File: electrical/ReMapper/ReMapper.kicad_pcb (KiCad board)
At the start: 4 copper layers, 76.7 x 45.3 mm, 46 parts, among them J2 USB_IN, J5 USB_OUT, U1 ESP32-S3-WROOM-1-N8R8, U2 RP2040, U3 W25Q128JVE, U5 W25Q128JVE, U6 SPX1117M3-L-3-3/TR, Y2 12MHZ

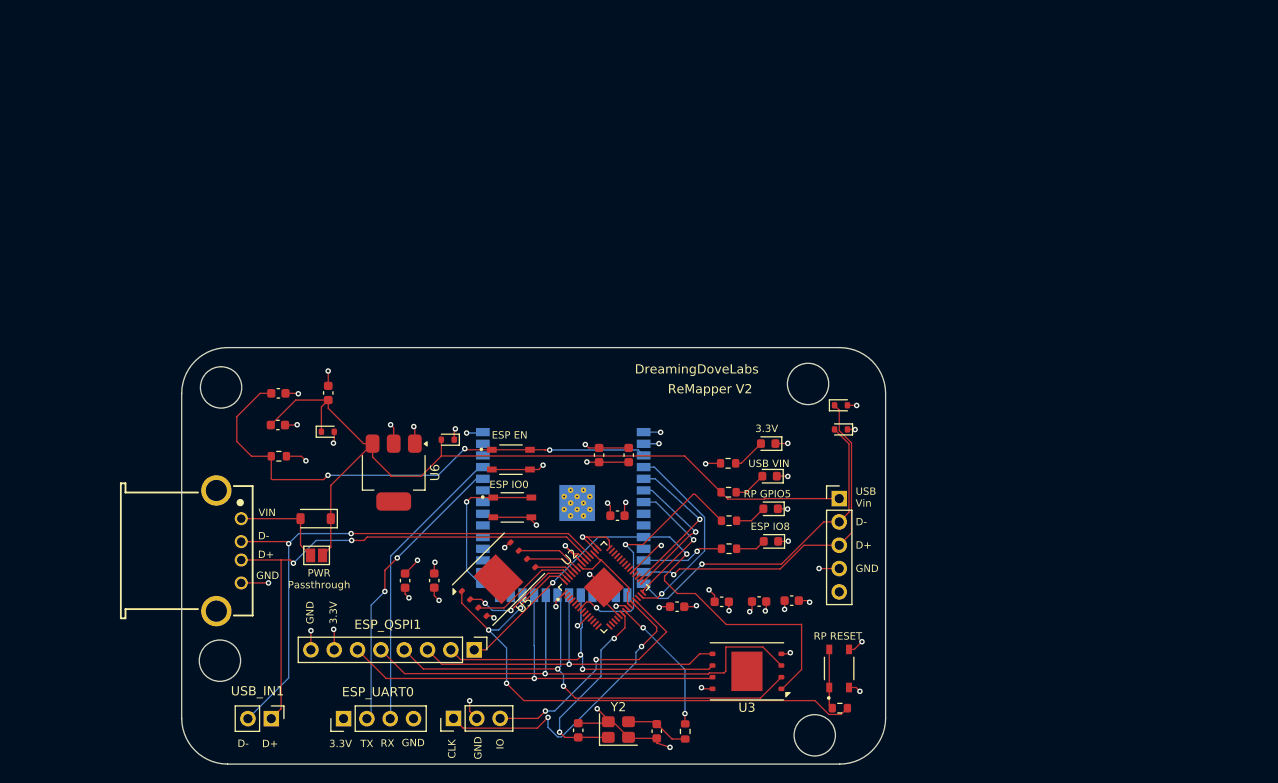
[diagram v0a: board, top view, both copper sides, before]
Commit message: schematic update, pcb design rules and blank slate on pcb editor
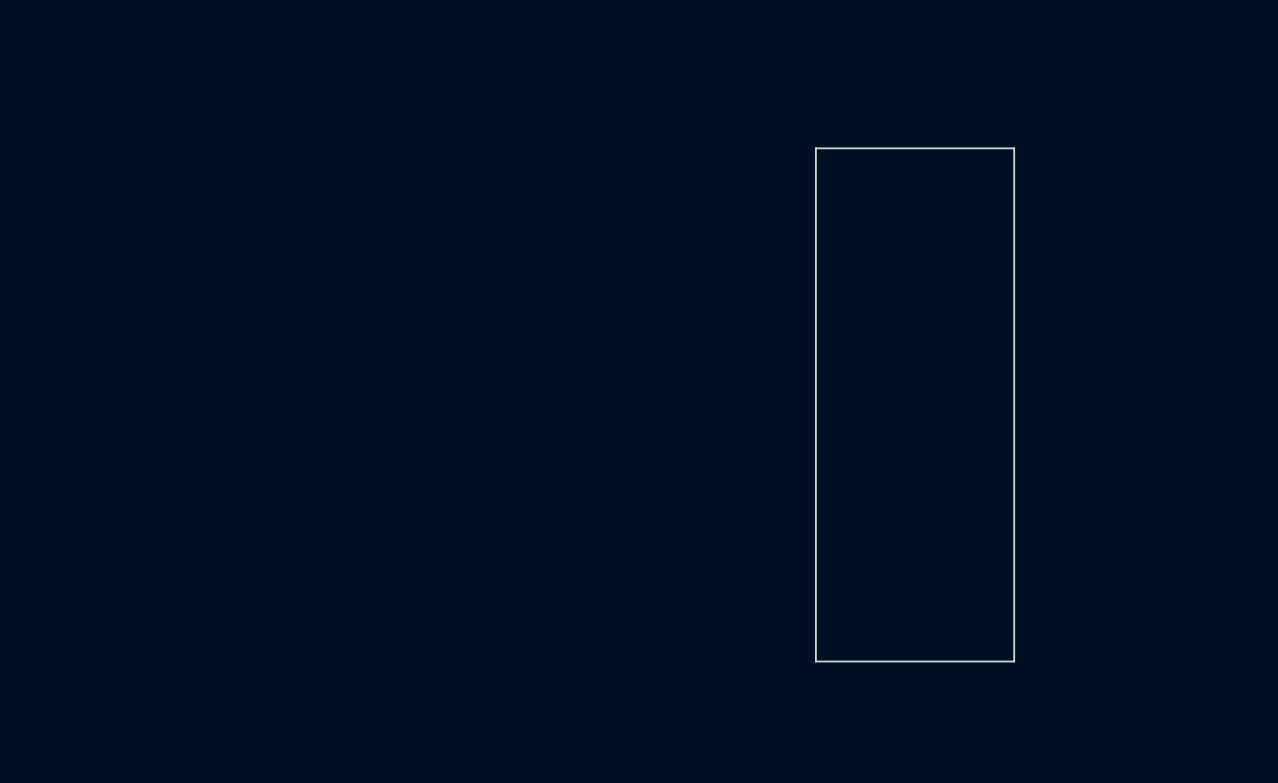
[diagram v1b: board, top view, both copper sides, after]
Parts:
- removed C1: 22uf, Capacitor_SMD:C_0603_1608Metric
- removed C10, C5: 100nf, Capacitor_SMD:C_0603_1608Metric
- removed C11, C12: 15 pF, Capacitor_SMD:C_0603_1608Metric
- removed C13, C4, C9: 2.2uf, Capacitor_SMD:C_0603_1608Metric
- removed C14, C16, C8: 47uF, Capacitor_SMD:C_0603_1608Metric
- removed C15, C2: 0.1uf, Capacitor_SMD:C_0603_1608Metric
- removed C3: 1uf, Capacitor_SMD:C_0603_1608Metric
- removed D1: D_Schottky, Diode_SMD:D_SOD-123
- removed D2, D3, D4, D5: ESD, Diode_SMD:D_SOD-523
- removed ESP_QSPI1: QSPI_Debug, Connector_PinHeader_2.54mm:PinHeader_1x08_P2.54mm_Vertical
- removed ESP_UART0: ESP_UART0, Connector_PinHeader_2.54mm:PinHeader_1x04_P2.54mm_Vertical
- removed J2: USB_IN, footprints:USBA_Female
- removed J5: USB_OUT, Connector_PinHeader_2.54mm:PinHeader_1x05_P2.54mm_Vertical
- removed JP1: VIN_Schottky, Jumper:SolderJumper-2_P1.3mm_Open_Pad1.0x1.5mm
- removed LED1: LED 33V, LED_SMD:LED_0603_1608Metric
- removed LED2: LED USB VIN, LED_SMD:LED_0603_1608Metric
- removed LED3, LED4: LED RP5, LED_SMD:LED_0603_1608Metric
- removed R1: 10k, Resistor_SMD:R_0603_1608Metric
- removed R3, R4: 1k, Resistor_SMD:R_0603_1608Metric
- removed R5, R6, R7, R8: 500, Resistor_SMD:R_0603_1608Metric
- removed RP_SWD1: SWD, Connector_PinHeader_2.54mm:PinHeader_1x03_P2.54mm_Vertical
- removed S1, S2, S3: SKRPABE010, footprints:push_button_SKRPABE010
- removed U1: ESP32-S3-WROOM-1-N8R8, RF_Module:ESP32-S3-WROOM-1
- removed U2: RP2040, footprints:rp2040
- removed U3, U5: W25Q128JVE, Package_SON:WSON-8-1EP_8x6mm_P1.27mm_EP3.4x4.3mm
- removed U6: SPX1117M3-L-3-3/TR, Package_TO_SOT_SMD:SOT-223
- removed USB_IN1: USB_IN_Debug, Connector_PinHeader_2.54mm:PinHeader_1x02_P2.54mm_Vertical
- removed Y2: 12MHZ, Crystal:Crystal_SMD_3225-4Pin_3.2x2.5mm
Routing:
- net /USB_VIN: track 90.8 -> 0.00 mm
- net GND: track 78.2 -> 0.00 mm, vias 35 -> 0
- net /QSPI_CS_rp: track 62.0 -> 0.00 mm, vias 3 -> 0
- net /USB_IN_D-: track 60.5 -> 0.00 mm, vias 2 -> 0
- net /QSPI_CS_esp: track 57.8 -> 0.00 mm, vias 2 -> 0
- net /USB_IN_D+: track 57.8 -> 0.00 mm, vias 2 -> 0
- net /QSPI_IO2_esp: track 56.9 -> 0.00 mm, vias 1 -> 0
- net Net-(U1-EN): track 56.7 -> 0.00 mm, vias 3 -> 0
- net /QSPI_IO1_esp: track 53.2 -> 0.00 mm, vias 2 -> 0
- net /3.3V: track 49.8 -> 0.00 mm, vias 21 -> 0
- net /QSPI_IO3_esp: track 49.1 -> 0.00 mm, vias 1 -> 0
- net /QSPI_IO0_esp: track 39.7 -> 0.00 mm, vias 1 -> 0
- net /USB_OUT_D+: track 39.3 -> 0.00 mm, vias 1 -> 0
- net /QSPI_CLK_esp: track 37.5 -> 0.00 mm, vias 2 -> 0
- net /USB_OUT_D-: track 36.6 -> 0.00 mm, vias 1 -> 0
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- removed copper zone on In2.Cu, net /3.3V
- removed copper zone on In1.Cu, net GND
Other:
- board size 76.7 x 45.3 mm -> 21.6 x 55.9 mm
- board text removed: "3.3V"
- board text removed: "CLK"
- board text removed: "D+"
- board text removed: "D-"
- board text removed: "DreamingDoveLabs"
- board text removed: "ESP EN"
- board text removed: "ESP IO0"
- board text removed: "ESP IO8"
- board text removed: "GND"
- board text removed: "IO"
- board text removed: "PWR Passthrough"
- board text removed: "RP GPIO5"
- board text removed: "RP RESET"
- board text removed: "RX"
- board text removed: "ReMapper V2"
- board text removed: "TX"
- board text removed: "USB VIN"
- board text removed: "USB Vin"
- board text removed: "VIN"

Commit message: started work on V3
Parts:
- added C1: 47uF, Capacitor_SMD:C_0603_1608Metric, F.Cu at (108.2, 60.0)
- added C10: 2.2uf, Capacitor_SMD:C_0603_1608Metric, F.Cu at (112.2, 67.6)
- added C11: 15 pF, Capacitor_SMD:C_0603_1608Metric, F.Cu at (112.2, 70.1)
- added C12: 15 pF, Capacitor_SMD:C_0603_1608Metric, F.Cu at (116.2, 60.0)
- added C13: 2.2uf, Capacitor_SMD:C_0603_1608Metric, F.Cu at (116.2, 62.6)
- added C14: 100nf, Capacitor_SMD:C_0603_1608Metric, F.Cu at (116.2, 65.1)
- added C2: 1uf, Capacitor_SMD:C_0603_1608Metric, B.Cu at (188.3, 64.4)
- added C3: 47uF, Capacitor_SMD:C_0603_1608Metric, F.Cu at (108.2, 62.6)
- added C4: 0.1uf, Capacitor_SMD:C_0603_1608Metric, F.Cu at (108.2, 65.1)
- added C5: 2.2uf, Capacitor_SMD:C_0603_1608Metric, F.Cu at (108.2, 67.6)
- added C6: 100nf, Capacitor_SMD:C_0603_1608Metric, F.Cu at (108.2, 70.1)
- added C7: 47uF, Capacitor_SMD:C_0603_1608Metric, F.Cu at (112.2, 60.0)
- added C8: 22uf, Capacitor_SMD:C_0603_1608Metric, B.Cu at (176.9, 60.8)
- added C9: 0.1uf, Capacitor_SMD:C_0603_1608Metric, B.Cu at (176.9, 63.0)
- added D1: ESD, Diode_SMD:D_SOD-523, F.Cu at (133.2, 60.0)
- added D2: ESD, Diode_SMD:D_SOD-523, F.Cu at (133.2, 62.5)
- added D3: ESD, Diode_SMD:D_SOD-523, B.Cu at (191.9, 66.7)
- added D4: ESD, Diode_SMD:D_SOD-523, B.Cu at (194.8, 66.7)
- added D5: D_Schottky, Diode_SMD:D_SOD-123, F.Cu at (97.7, 76.5)
- added J1: ESP_UART0, Connector_PinHeader_2.54mm:PinHeader_1x04_P2.54mm_Vertical, F.Cu at (124.5, 61.1)
- added J2: I2C Display, Connector_PinHeader_2.54mm:PinHeader_1x04_P2.54mm_Vertical, F.Cu at (129.1, 61.1)
- added J3: USB_IN, footprints:USBA_Female, F.Cu at (111.1, 50.9)
- added J4: USB_OUT, Connector_PinHeader_2.54mm:PinHeader_1x05_P2.54mm_Vertical, F.Cu at (132.5, 45.2)
- added J5: Programming Mode SW, Connector_PinHeader_2.54mm:PinHeader_1x02_P2.54mm_Vertical, F.Cu at (118.3, 73.6)
- added JP1: VIN_Schottky, Jumper:SolderJumper-2_P1.3mm_Open_Pad1.0x1.5mm, F.Cu at (97.0, 73.0)
- added LED1: LED 33V, LED_SMD:LED_0603_1608Metric, F.Cu at (104.2, 60.1)
- added LED2: LED RP5, LED_SMD:LED_0603_1608Metric, F.Cu at (104.2, 62.7)
- added LED3: LED RP5, LED_SMD:LED_0603_1608Metric, F.Cu at (104.2, 65.3)
- added LED4: LED RP5, LED_SMD:LED_0603_1608Metric, F.Cu at (104.2, 67.9)
- added LED5: LED RP5, LED_SMD:LED_0603_1608Metric, F.Cu at (104.2, 70.4)
- added R1: 10k, Resistor_SMD:R_0603_1608Metric, B.Cu at (176.9, 65.2)
- added R2: 1k, Resistor_SMD:R_0603_1608Metric, F.Cu at (116.2, 67.6)
- added R3: 500, Resistor_SMD:R_0603_1608Metric, F.Cu at (116.2, 70.1)
- added R4: 500, Resistor_SMD:R_0603_1608Metric, F.Cu at (120.2, 60.0)
- added R5: 1k, Resistor_SMD:R_0603_1608Metric, F.Cu at (120.2, 62.6)
- added R6: 500, Resistor_SMD:R_0603_1608Metric, F.Cu at (120.2, 65.1)
- added R7: 500, Resistor_SMD:R_0603_1608Metric, F.Cu at (120.2, 67.6)
- added R8: 500, Resistor_SMD:R_0603_1608Metric, F.Cu at (120.2, 70.1)
- added S1: SKRPABE010, footprints:push_button_SKRPABE010, B.Cu at (183.6, 67.1)
- added S2: SKRPABE010, footprints:push_button_SKRPABE010, B.Cu at (183.6, 61.7)
- added S3: SKRPABE010, footprints:push_button_SKRPABE010, F.Cu at (98.7, 50.1)
- added S4: ESP BUTTON 3, footprints:push_button_SKRPABE010, F.Cu at (98.7, 54.8)
- added S5: ESP BUTTON 1, footprints:push_button_SKRPABE010, F.Cu at (98.7, 59.6)
- added S6: ESP BUTTON 2, footprints:push_button_SKRPABE010, F.Cu at (98.7, 64.3)
- added U1: SPX1117M3-L-3-3/TR, Package_TO_SOT_SMD:SOT-223, F.Cu at (111.1, 75.5)
- added U2: W25Q128JVE, Package_SON:WSON-8-1EP_8x6mm_P1.27mm_EP3.4x4.3mm, F.Cu at (125.4, 46.7)
- added U3: ESP32-S3-WROOM-1-N8R8, RF_Module:ESP32-S3-WROOM-1, B.Cu at (180.0, 80.2)
- added U4: RP2040, footprints:rp2040, F.Cu at (127.4, 75.6)
- added U5: W25Q128JVE, Package_SON:WSON-8-1EP_8x6mm_P1.27mm_EP3.4x4.3mm, F.Cu at (125.4, 54.3)
- added Y1: 12MHZ, Crystal:Crystal_SMD_3225-4Pin_3.2x2.5mm, F.Cu at (97.4, 69.0)
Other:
- board size 21.6 x 55.9 mm -> 32 x 55 mm

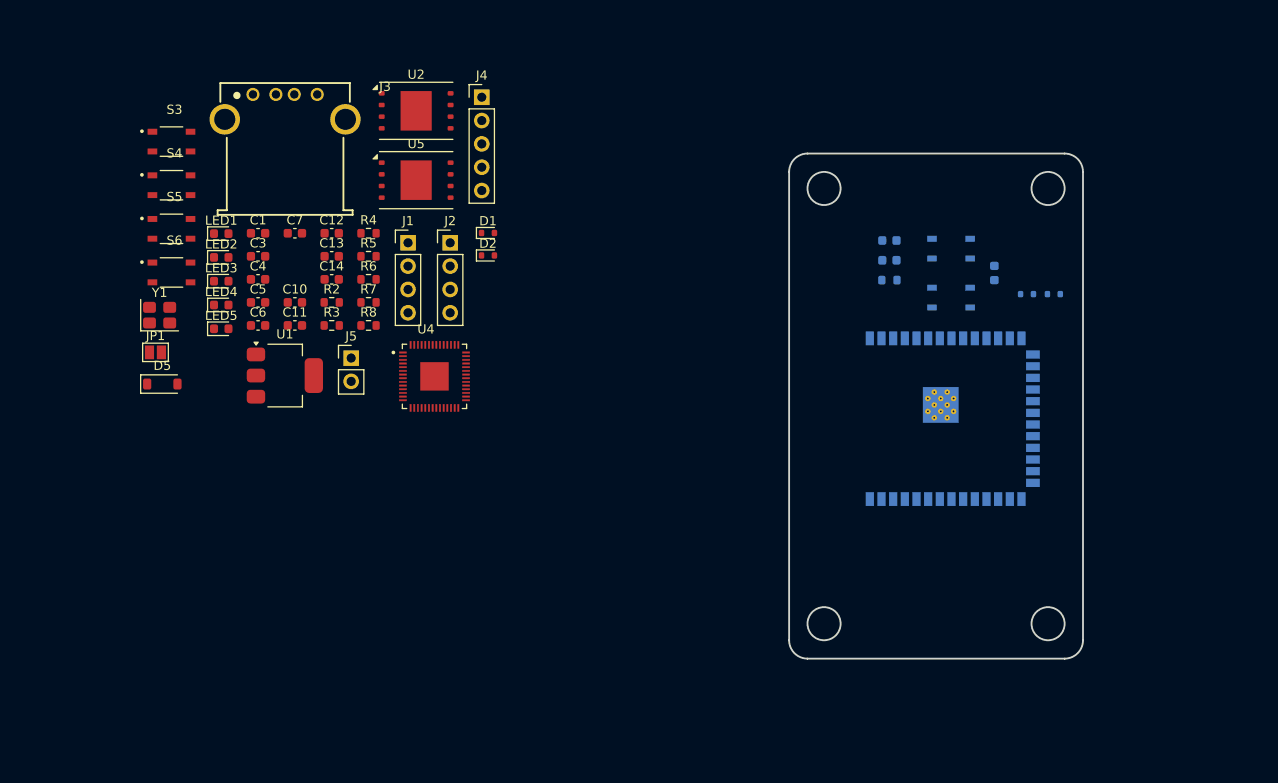
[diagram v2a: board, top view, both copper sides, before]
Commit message: more component placement, removed lots of debug and hmi
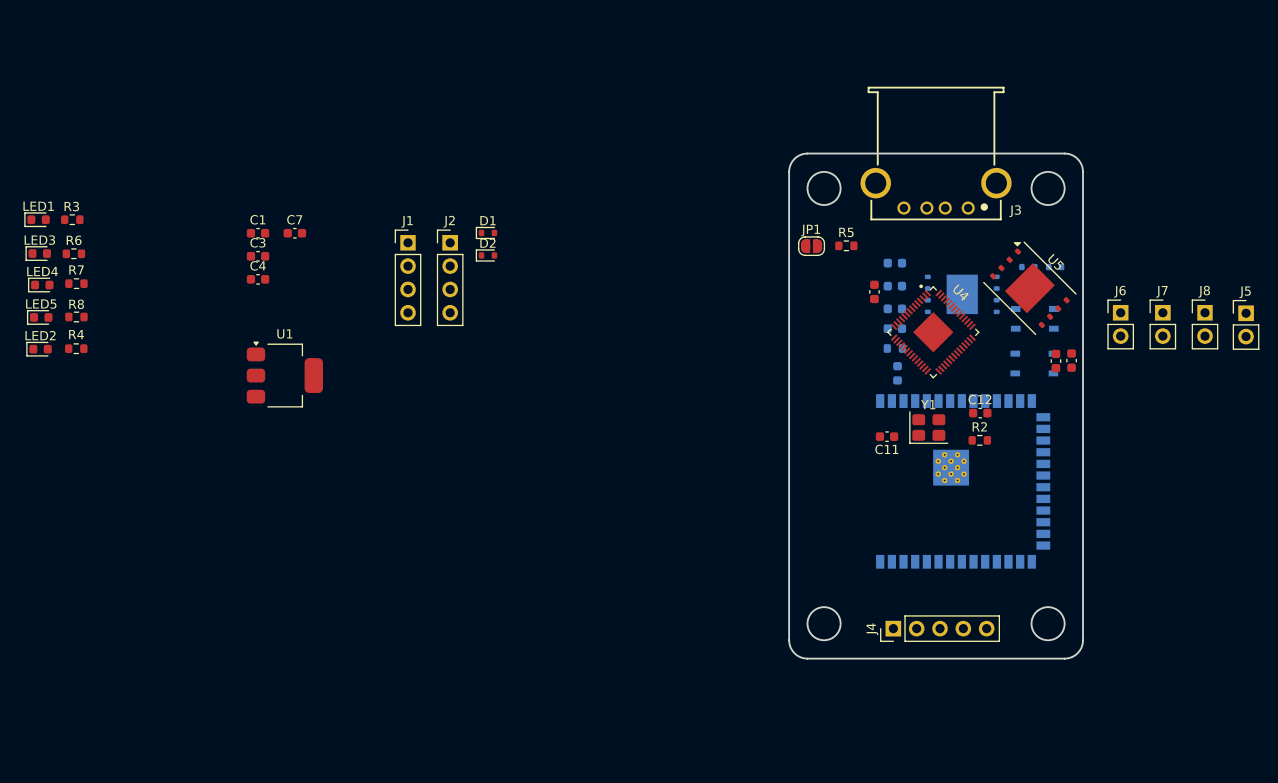
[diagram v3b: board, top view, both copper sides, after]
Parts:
- removed D5: D_Schottky, Diode_SMD:D_SOD-123
- removed S3: SKRPABE010, footprints:push_button_SKRPABE010
- removed S4: ESP BUTTON 3, footprints:push_button_SKRPABE010
- removed S5: ESP BUTTON 1, footprints:push_button_SKRPABE010
- removed S6: ESP BUTTON 2, footprints:push_button_SKRPABE010
- added J6: Button 1, Connector_PinHeader_2.54mm:PinHeader_1x02_P2.54mm_Vertical, F.Cu at (202.1, 68.7)
- added J7: Button 2, Connector_PinHeader_2.54mm:PinHeader_1x02_P2.54mm_Vertical, F.Cu at (206.7, 68.7)
- added J8: Button 3, Connector_PinHeader_2.54mm:PinHeader_1x02_P2.54mm_Vertical, F.Cu at (211.3, 68.7)
- C5, C6, U2: moved to B.Cu
- J5: value Programming Mode SW -> ESP Prog Mode
- JP1: value VIN_Schottky -> RP2040 Prog; footprint Jumper:SolderJumper-2_P1.3mm_Open_Pad1.0x1.5mm -> Jumper:SolderJumper-2_P1.3mm_Open_RoundedPad1.0x1.5mm
- moved J5 97.6 mm to (215.7, 68.8)
- moved Y1 84.6 mm to (181.2, 81.2)
- moved C14 81.0 mm to (196.7, 73.9), turned to -90 degrees
- moved C13 79.7 mm to (195.0, 74.0), turned to -90 degrees
- moved C12 73.3 mm to (186.8, 79.6)
- moved J4 73.2 mm to (177.3, 103.1), turned to 90 degrees
- moved JP1 72.4 mm to (168.4, 61.5)
- moved R2 72.2 mm to (186.8, 82.6)
- moved J3 70.9 mm to (182.0, 51.4), turned to 180 degrees
- moved C6 69.7 mm to (177.5, 63.3)
- moved C5 69.4 mm to (177.5, 65.8)
- moved U5 67.9 mm to (192.2, 66.0), turned to -45 degrees
- moved C11 65.6 mm to (176.7, 82.2), turned to 180 degrees
- moved C10 63.1 mm to (175.3, 66.4), turned to 90 degrees
- moved U2 62.7 mm to (184.8, 66.7)
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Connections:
- J3 pad 1: Net-(D5-A) -> /USB_VIN
- JP1 pad 1: Net-(D5-A) -> GND
- JP1 pad 2: /USB_VIN -> Net-(JP1-B)
- R5 pad 1: Net-(R5-Pad1) -> Net-(JP1-B)

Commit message: first layout attempt, had to compromise on some SMD and shrink the header pins
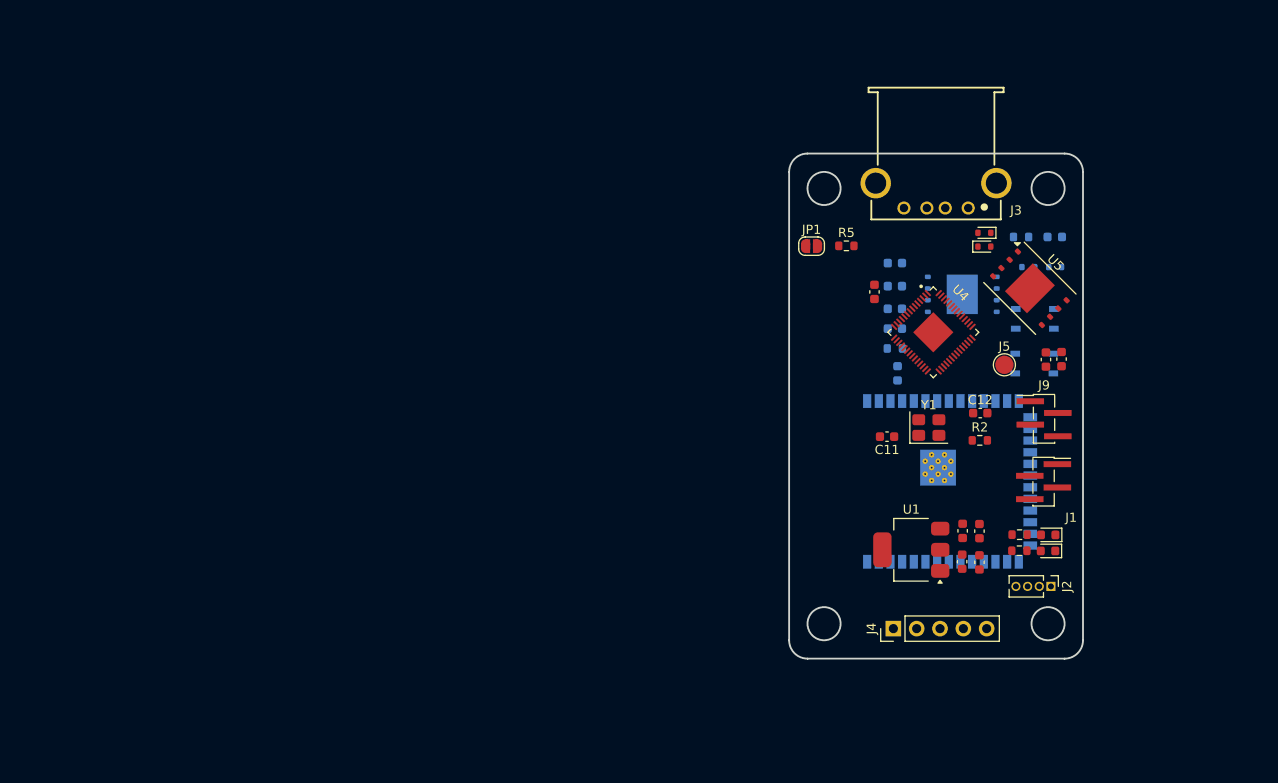
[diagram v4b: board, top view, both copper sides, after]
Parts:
- removed J6: Button 1, Connector_PinHeader_2.54mm:PinHeader_1x02_P2.54mm_Vertical
- removed J7: Button 2, Connector_PinHeader_2.54mm:PinHeader_1x02_P2.54mm_Vertical
- removed J8: Button 3, Connector_PinHeader_2.54mm:PinHeader_1x02_P2.54mm_Vertical
- removed LED2, LED4: LED RP5, LED_SMD:LED_0603_1608Metric
- removed R4, R7: 500, Resistor_SMD:R_0603_1608Metric
- added J9: Button Socket, Connector_PinHeader_1.27mm:PinHeader_1x04_P1.27mm_Vertical_SMD_Pin1Left, F.Cu at (193.8, 80.2)
- J1: footprint Connector_PinHeader_2.54mm:PinHeader_1x04_P2.54mm_Vertical -> Connector_PinHeader_1.27mm:PinHeader_1x04_P1.27mm_Vertical_SMD_Pin1Right
- J2: footprint Connector_PinHeader_2.54mm:PinHeader_1x04_P2.54mm_Vertical -> Connector_PinHeader_1.27mm:PinHeader_1x04_P1.27mm_Vertical
- J5: value ESP Prog Mode -> Button GND Pad; footprint Connector_PinHeader_2.54mm:PinHeader_1x02_P2.54mm_Vertical -> TestPoint:TestPoint_Pad_D2.0mm
- LED1, R3: moved to B.Cu
- moved LED3 114.5 mm to (194.2, 94.6), turned to 180 degrees
- moved LED5 112.2 mm to (194.2, 92.9), turned to 180 degrees
- moved LED1 110.7 mm to (194.9, 60.5), turned to 180 degrees
- moved R6 107.9 mm to (191.1, 94.6), turned to 0 degrees
- moved R8 105.4 mm to (191.1, 92.9), turned to 0 degrees
- moved R3 103.3 mm to (191.2, 60.5), turned to 0 degrees
- moved C1 86.3 mm to (186.7, 95.9), turned to -90 degrees
- moved C4 82.6 mm to (184.8, 95.8), turned to -90 degrees
- moved C3 82.3 mm to (184.9, 92.5), turned to -90 degrees
- moved C7 81.3 mm to (186.7, 92.5), turned to -90 degrees
- moved J2 75.4 mm to (194.5, 98.5), turned to -90 degrees
- moved J1 73.9 mm to (193.7, 87.1)
- moved U1 70.8 mm to (179.3, 94.5), turned to 180 degrees
- moved D2 54.1 mm to (187.2, 61.5)
- moved D1 54.1 mm to (187.2, 60.0), turned to 180 degrees
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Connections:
- U3 pad 17: /LED_ESP_2 -> unconnected-(U3-IO9-Pad17)
- U4 pad 8: /LED_RP_2 -> unconnected-(U4-GPIO6-Pad8)
